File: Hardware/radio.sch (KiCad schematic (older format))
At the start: 4 parts

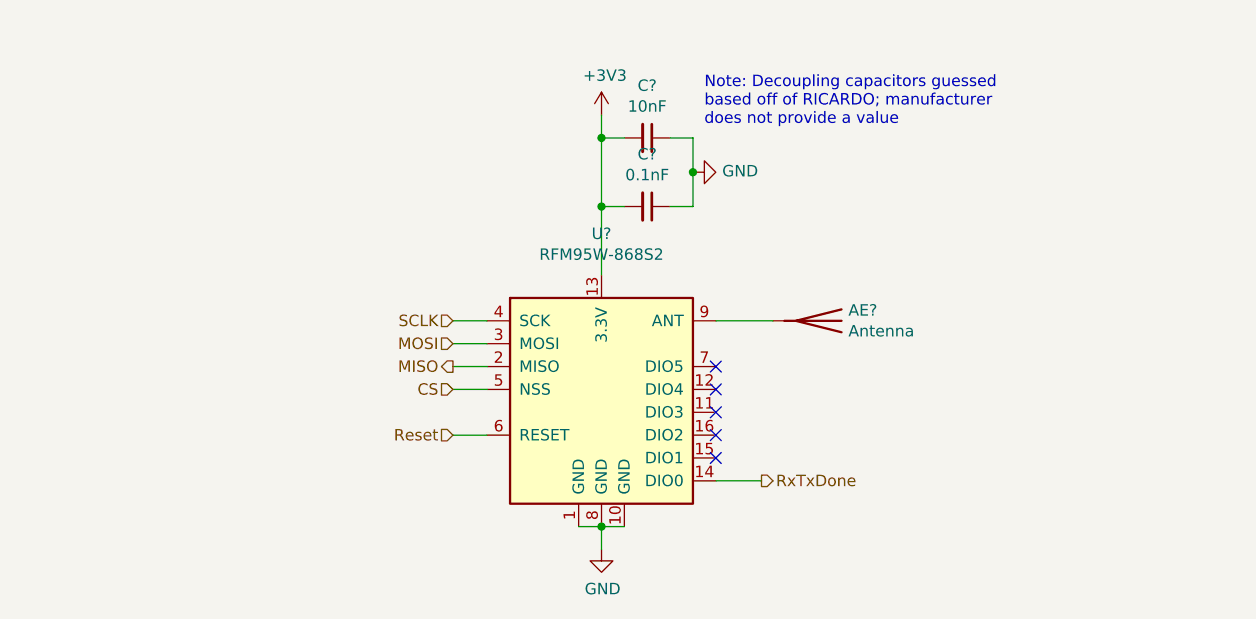
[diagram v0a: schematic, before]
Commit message: Added activity LEDs for SD and radio
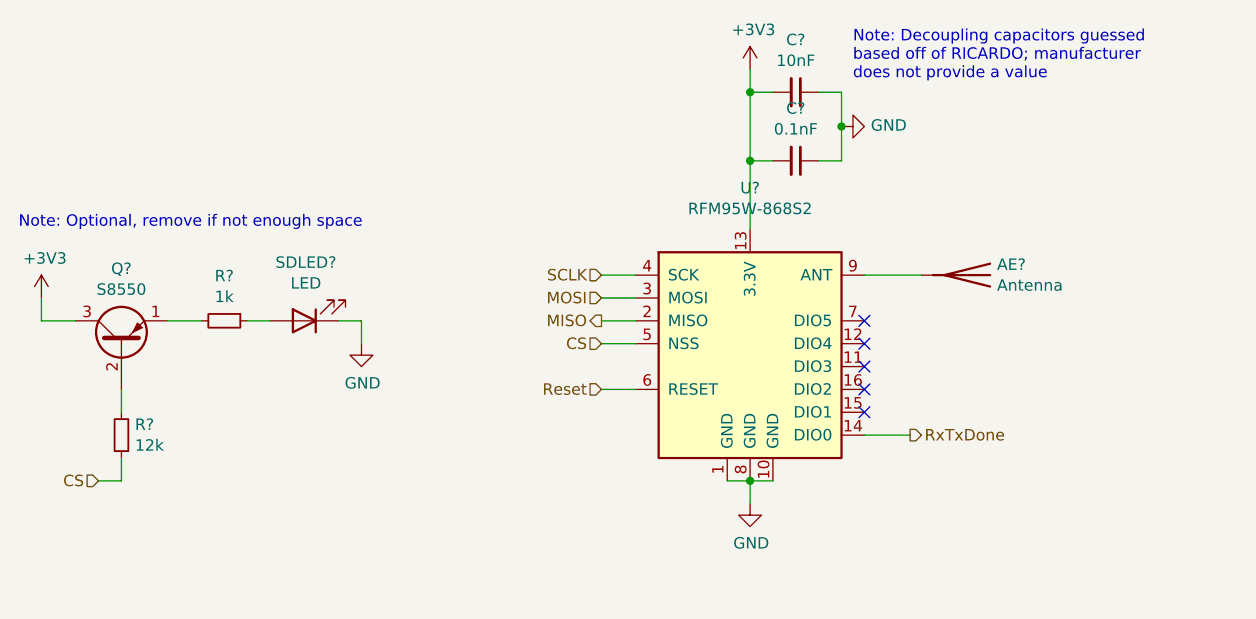
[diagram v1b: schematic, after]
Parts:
- added Q?: S8550, Package_TO_SOT_THT:TO-92_Inline, symbol Transistor_BJT:S8550
- added R?: 1k, symbol Device:R_Small
- added R?: 12k, symbol Device:R_Small
- added RadioLED?: LED, symbol Device:LED
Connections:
- net +3V3: now also Q?.3 (C)
- net CS: now also R?.1
- net GND: now also RadioLED?.1 (K)
- new net: R?.1, RadioLED?.2 (A)
- new net: Q?.1 (E), R?.2
- new net: Q?.2 (B), R?.2
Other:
- note added: "Note: Optional, remove if not enough space"
- moved on the sheet: AE?, C?, U?
